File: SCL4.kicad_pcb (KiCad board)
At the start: 2 copper layers, 233.7 x 300 mm, 4 parts

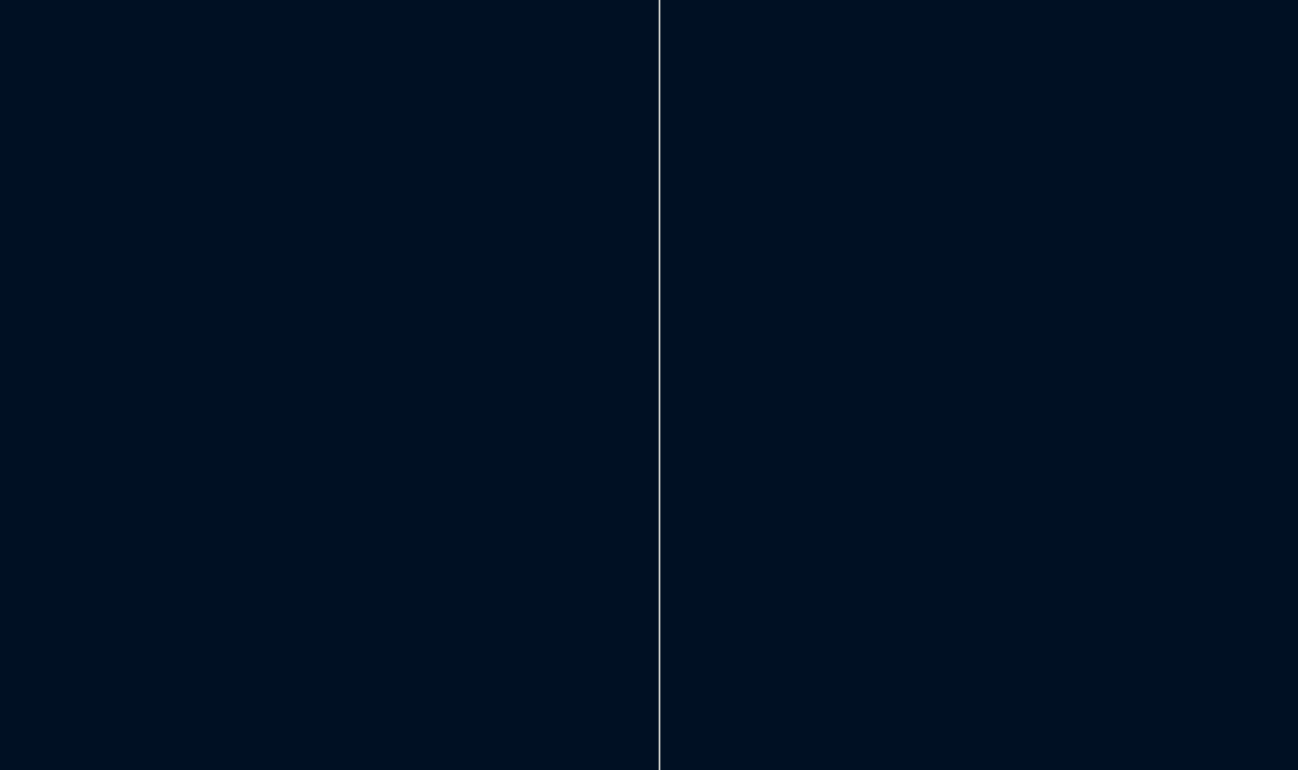
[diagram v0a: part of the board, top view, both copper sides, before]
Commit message: swap abcd on siedecon
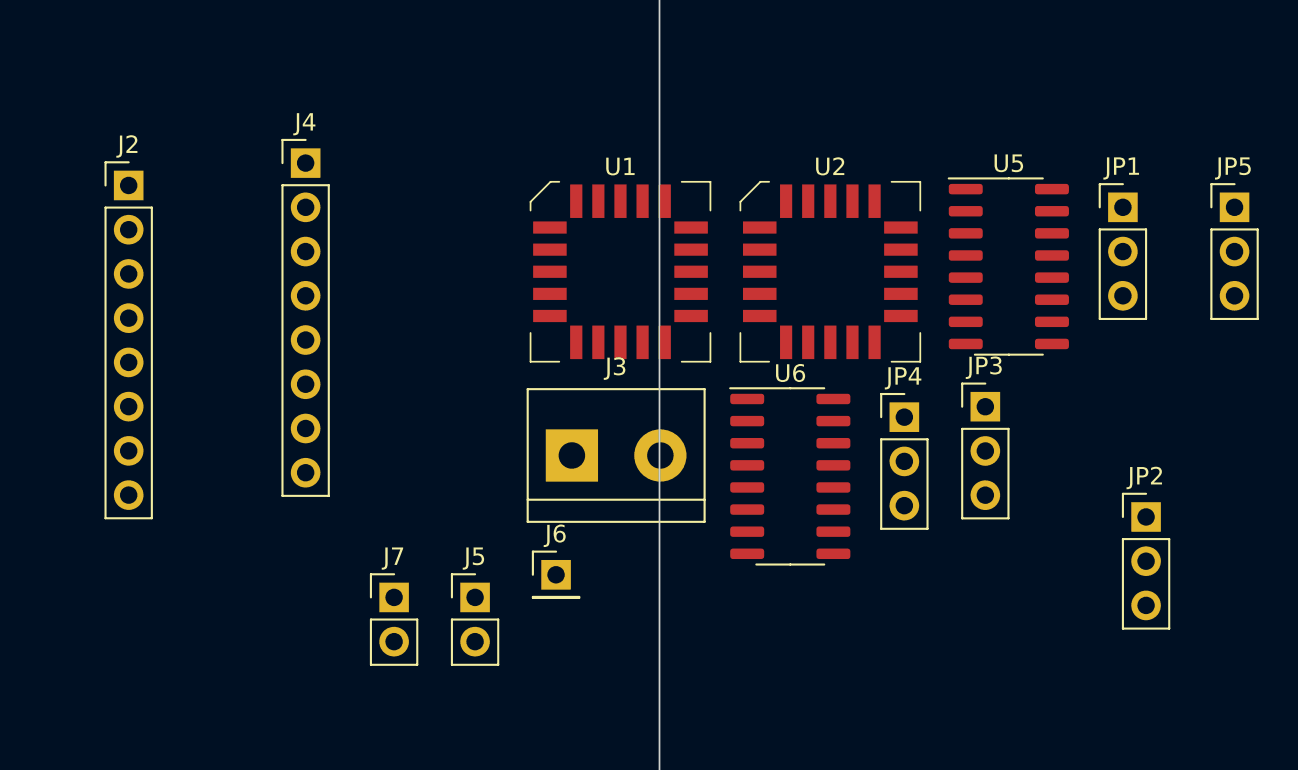
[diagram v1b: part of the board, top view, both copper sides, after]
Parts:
- added J2: Conn_01x08, Connector_PinHeader_2.54mm:PinHeader_1x08_P2.54mm_Vertical, F.Cu at (203.2, 21.6)
- added J3: 5V out, TerminalBlock:TerminalBlock_bornier-2_P5.08mm, F.Cu at (228.7, 37.1)
- added J4: spare1, Connector_PinHeader_2.54mm:PinHeader_1x08_P2.54mm_Vertical, F.Cu at (213.4, 20.3)
- added J5: SP1, Connector_PinHeader_2.54mm:PinHeader_1x02_P2.54mm_Vertical, F.Cu at (223.1, 45.3)
- added J6: spare2, Connector_PinHeader_2.54mm:PinHeader_1x01_P2.54mm_Vertical, F.Cu at (227.7, 44.0)
- added J7: SP2, Connector_PinHeader_2.54mm:PinHeader_1x02_P2.54mm_Vertical, F.Cu at (218.4, 45.3)
- added JP1: LSA, Connector_PinHeader_2.54mm:PinHeader_1x03_P2.54mm_Vertical, F.Cu at (260.3, 22.9)
- added JP2: LSB, Connector_PinHeader_2.54mm:PinHeader_1x03_P2.54mm_Vertical, F.Cu at (261.6, 40.6)
- added JP3: LOCAL, Connector_PinHeader_2.54mm:PinHeader_1x03_P2.54mm_Vertical, F.Cu at (252.4, 34.3)
- added JP4: NEXT, Connector_PinHeader_2.54mm:PinHeader_1x03_P2.54mm_Vertical, F.Cu at (247.7, 34.9)
- added JP5: SYSTEM, Connector_PinHeader_2.54mm:PinHeader_1x03_P2.54mm_Vertical, F.Cu at (266.7, 22.9)
- added U1: MC10H125 (20PLCC), Package_LCC:PLCC-20, F.Cu at (231.4, 26.6)
- added U2: MC10H124 (20PLCC), Package_LCC:PLCC-20, F.Cu at (243.5, 26.6)
- added U5: MC3487DX, Package_SO:SOIC-16_3.9x9.9mm_P1.27mm, F.Cu at (253.7, 26.3)
- added U6: MC3487DX, Package_SO:SOIC-16_3.9x9.9mm_P1.27mm, F.Cu at (241.2, 38.3)

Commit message: starting routing
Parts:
- added C2: 100uF 63V, Capacitor_THT:CP_Radial_D10.0mm_P5.00mm, F.Cu at (259.3, 182.2)
- added D1: SMCX70A, Diode_SMD:D_SMC_Handsoldering, F.Cu at (253.4, 157.5)
- added D2: SMCX70A, Diode_SMD:D_SMC_Handsoldering, F.Cu at (266.1, 149.2)
- added F1: 5A, BUSSMAN:BUSSMAN SFT-1, F.Cu at (275.0, 166.2)
- added F2: 3A, BUSSMAN:BUSSMAN SFT-1, F.Cu at (275.0, 157.9)
- added J3: Siemens_A1010-A263, SIEDECON:Siedecon 256+6, F.Cu at (291.9, 27.9)
- added L1: INDUCTOR, Inductor_THT:L_Axial_L12.8mm_D5.8mm_P20.32mm_Horizontal_Fastron_HBCC, F.Cu at (246.4, 162.6)
- added R1: 10R 2%, Resistor_THT:R_Axial_DIN0207_L6.3mm_D2.5mm_P15.24mm_Horizontal, F.Cu at (252.7, 182.9)
- added R10: 10K, Resistor_SMD:R_2816_7142Metric_Pad3.20x4.45mm_HandSolder, F.Cu at (263.5, 68.6)
- added R2: 27R, Resistor_SMD:R_1206_3216Metric_Pad1.30x1.75mm_HandSolder, F.Cu at (287.0, 228.6)
- added R3: 51R, Resistor_SMD:R_2816_7142Metric_Pad3.20x4.45mm_HandSolder, F.Cu at (263.5, 76.2)
- added R4: 51R, Resistor_SMD:R_2816_7142Metric_Pad3.20x4.45mm_HandSolder, F.Cu at (251.5, 53.3)
- added R5: 51R, Resistor_SMD:R_2816_7142Metric_Pad3.20x4.45mm_HandSolder, F.Cu at (263.5, 53.3)
- added R6: 51R, Resistor_SMD:R_2816_7142Metric_Pad3.20x4.45mm_HandSolder, F.Cu at (251.5, 61.0)
- added R7: 51R, Resistor_SMD:R_2816_7142Metric_Pad3.20x4.45mm_HandSolder, F.Cu at (251.5, 68.6)
- added R8: 51R, Resistor_SMD:R_2816_7142Metric_Pad3.20x4.45mm_HandSolder, F.Cu at (251.5, 76.2)
- added R9: 10K, Resistor_SMD:R_2816_7142Metric_Pad3.20x4.45mm_HandSolder, F.Cu at (263.5, 61.0)
- added U3: TRAM Size 2, Transputer:TRAM size 2, F.Cu at (243.8, 27.3)
- C1: renamed from C2; footprint Capacitor_THT:CP_Axial_L29.0mm_D20.0mm_P35.00mm_Horizontal -> Capacitor_THT:CP_Radial_D5.0mm_P2.50mm
- C3: renamed from C1; footprint Capacitor_THT:CP_Axial_L26.5mm_D20.0mm_P33.00mm_Horizontal -> Capacitor_THT:CP_Radial_D13.0mm_P5.00mm
- J1: renamed from J4; footprint Connector_PinHeader_2.54mm:PinHeader_1x08_P2.54mm_Vertical -> Connector_PinHeader_2.54mm:PinHeader_1x01_P2.54mm_Vertical
- moved C1 200.4 mm to (246.4, 139.7)
- moved PS1 180.2 mm to (238.7, 127.1), turned to -90 degrees
- moved PS2 149.4 mm to (264.2, 215.9), turned to -90 degrees
- moved J1 109.2 mm to (273.1, 111.8)
- moved J5 91.9 mm to (281.9, 111.8)
- moved J2 89.6 mm to (286.4, 111.8)
- moved J4 85.9 mm to (277.5, 111.8)
- moved C3 85.6 mm to (264.2, 167.6)
- moved U1 76.4 mm to (276.9, 99.1)
- moved JP3 74.4 mm to (256.5, 96.5)
- moved JP1 64.5 mm to (266.7, 96.5)
- moved JP2 62.9 mm to (261.6, 96.5)
- moved J7 62.1 mm to (180.3, 76.2), turned to -90 degrees
- moved U2 52.0 mm to (276.9, 76.2)
- moved U4 45.4 mm to (276.9, 25.4), turned to -90 degrees
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- renumbered J6 to J2, J5 to J4, J7 to J5, J2 to J6, J3 to J7, JP4 to JP1, JP3 to JP2, JP5 to JP3, JP1 to JP4, JP2 to JP5, U5 to U1, U6 to U2, U1 to U4, U2 to U5
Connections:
- C1 pad 1: +48V -> Net-(C1-Pad1)
- PS1 pad 1: +48V -> Net-(C1-Pad1)
- PS2 pad 14: Net-(PS2-Pad14) -> GND
- PS2 pad 15: Net-(PS2-Pad14) -> GND
- PS2 pad 16: Net-(PS2-Pad14) -> GND
- PS2 pad 17: unconnected-(PS2-Pad17) -> Net-(R2-Pad1)
- PS2 pad 18: -5V -> Net-(PS2-Pad18)
- PS2 pad 19: -5V -> Net-(PS2-Pad18)
- PS2 pad 20: -5V -> Net-(PS2-Pad18)
- PS2 pad 32: +48V -> +L48V
- PS2 pad 33: -48V -> -L48V
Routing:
- net GND: track 47.7 -> 787.7 mm, vias 0 -> 1
- net +5V: track 47.0 -> 473.5 mm, vias 0 -> 1
- net Net-(C1-Pad1): track 0.00 -> 116.8 mm
- net /TByte: track 0.00 -> 107.1 mm, vias 0 -> 1
- net /TL0In: track 0.00 -> 80.6 mm
- net +L48V: track 0.00 -> 77.7 mm
- net /TL0Out: track 0.00 -> 77.0 mm
- net /TNotError: track 0.00 -> 65.8 mm
- net -L48V: track 0.00 -> 60.0 mm
- net /TL2out: track 0.00 -> 49.8 mm, vias 0 -> 1
- net +48V: track 121.0 -> 71.8 mm
- net /TClk: track 0.00 -> 46.2 mm
- net //L2OUT: track 0.00 -> 40.5 mm, vias 0 -> 2
- net //L2IN: track 0.00 -> 38.6 mm, vias 0 -> 2
- net /RESET: track 0.00 -> 31.4 mm, vias 0 -> 1
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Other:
- board size 233.7 x 300 mm -> 280 x 234 mm

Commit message: board layout complete
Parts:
- R10, R3, R4, R5, R6, R7, R8, R9: footprint Resistor_SMD:R_2816_7142Metric_Pad3.20x4.45mm_HandSolder -> Resistor_SMD:R_1206_3216Metric_Pad1.30x1.75mm_HandSolder
- moved R3 46.6 mm to (268.6, 29.8), turned to 90 degrees
- moved R10 42.6 mm to (261.6, 26.0), turned to 180 degrees
- moved R5 31.5 mm to (284.5, 29.8), turned to -90 degrees
- moved R8 30.1 mm to (280.0, 66.7), turned to 180 degrees
- moved R6 28.6 mm to (280.0, 61.6), turned to 180 degrees
- moved R4 25.9 mm to (273.7, 66.7)
- moved R7 23.3 mm to (273.7, 61.6)
- moved R9 18.1 mm to (257.8, 43.8), turned to 180 degrees
- moved D2 10.8 mm to (257.8, 142.2), turned to 180 degrees
- moved D1 7.24 mm to (257.8, 151.8), turned to 180 degrees
- moved C2 6.31 mm to (265.4, 181.0), turned to 180 degrees
- moved C3 5.99 mm to (259.1, 164.5), turned to 0 degrees
- moved J7 3.81 mm to (184.2, 76.2)
- moved C1 2.62 mm to (245.7, 137.2)
- moved U3 2.54 mm to (246.4, 27.3)
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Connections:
- net +L48V renamed Net-(C2-Pad1)
- net -L48V renamed Net-(C2-Pad2)
- net Net-(J5-Pad1) renamed +5Vbig
- net Net-(JP4-Pad2) renamed /SpeedA
- net Net-(JP5-Pad2) renamed /SpeedB
- PS2 pad 1: unconnected-(PS2-Pad1) -> (no net)
- PS2 pad 10: unconnected-(PS2-Pad10) -> (no net)
- PS2 pad 11: unconnected-(PS2-Pad11) -> (no net)
- PS2 pad 12: unconnected-(PS2-Pad12) -> (no net)
- PS2 pad 13: unconnected-(PS2-Pad13) -> (no net)
- PS2 pad 18: Net-(PS2-Pad18) -> -5V
- PS2 pad 19: Net-(PS2-Pad18) -> -5V
- PS2 pad 2: unconnected-(PS2-Pad2) -> (no net)
- PS2 pad 20: Net-(PS2-Pad18) -> -5V
- PS2 pad 21: unconnected-(PS2-Pad21) -> (no net)
- PS2 pad 22: unconnected-(PS2-Pad22) -> (no net)
- PS2 pad 23: unconnected-(PS2-Pad23) -> (no net)
- PS2 pad 24: unconnected-(PS2-Pad24) -> (no net)
- PS2 pad 26: unconnected-(PS2-Pad26) -> (no net)
- PS2 pad 27: unconnected-(PS2-Pad27) -> (no net)
- PS2 pad 28: unconnected-(PS2-Pad28) -> (no net)
- PS2 pad 29: unconnected-(PS2-Pad29) -> (no net)
- PS2 pad 3: unconnected-(PS2-Pad3) -> (no net)
- PS2 pad 30: unconnected-(PS2-Pad30) -> (no net)
- PS2 pad 31: unconnected-(PS2-Pad31) -> (no net)
- PS2 pad 34: unconnected-(PS2-Pad34) -> (no net)
- PS2 pad 35: unconnected-(PS2-Pad35) -> (no net)
- PS2 pad 36: unconnected-(PS2-Pad36) -> (no net)
- PS2 pad 37: unconnected-(PS2-Pad37) -> (no net)
- PS2 pad 38: unconnected-(PS2-Pad38) -> (no net)
- PS2 pad 39: unconnected-(PS2-Pad39) -> (no net)
- PS2 pad 4: unconnected-(PS2-Pad4) -> (no net)
- PS2 pad 40: unconnected-(PS2-Pad40) -> (no net)
- PS2 pad 5: unconnected-(PS2-Pad5) -> (no net)
- PS2 pad 6: unconnected-(PS2-Pad6) -> (no net)
- PS2 pad 7: unconnected-(PS2-Pad7) -> (no net)
- PS2 pad 8: unconnected-(PS2-Pad8) -> (no net)
- PS2 pad 9: unconnected-(PS2-Pad9) -> (no net)
- R10 pad 2: Net-(R10-Pad2) -> GND
- R4 pad 2: GND -> -5V
- R6 pad 2: GND -> -5V
- R7 pad 2: GND -> -5V
- R8 pad 2: GND -> -5V
- R9 pad 2: Net-(R10-Pad2) -> GND
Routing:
- net -5V: track 28.7 -> 290.6 mm, vias 0 -> 6
- net /TReset: track 0.00 -> 140.5 mm, vias 0 -> 2
- net /TAnalyse: track 0.00 -> 137.6 mm, vias 0 -> 2
- net +5V: track 473.5 -> 600.7 mm, vias 1 -> 4
- net /TL3in: track 0.00 -> 113.2 mm, vias 0 -> 4
- net /TL3out: track 0.00 -> 99.1 mm
- net GND: track 787.7 -> 883.5 mm, vias 1 -> 6
- net Net-(JP3-Pad2): track 0.00 -> 50.3 mm, vias 0 -> 2
- net /TL2in: track 0.00 -> 49.0 mm, vias 0 -> 2
- net /TL0In: track 80.6 -> 105.8 mm
- net /TNotError: track 65.8 -> 90.3 mm, vias 0 -> 1
- net /TL0Out: track 77.0 -> 100.4 mm
- net /L2OUT: track 30.5 -> 52.2 mm, vias 2 -> 3
- net //L3OUT: track 24.7 -> 41.8 mm, vias 0 -> 2
- net -48V: track 172.0 -> 156.7 mm
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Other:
- board size 280 x 234 mm -> 127.6 x 233.3 mm
- board text added: "!ERROR"
- board text added: "+5V"
- board text added: "ANALYSE"
- board text added: "BYTE"
- board text added: "CLOCK"
- board text added: "GND"
- board text added: "L0 IN"
- board text added: "L0 OUT"
- board text added: "RESET"

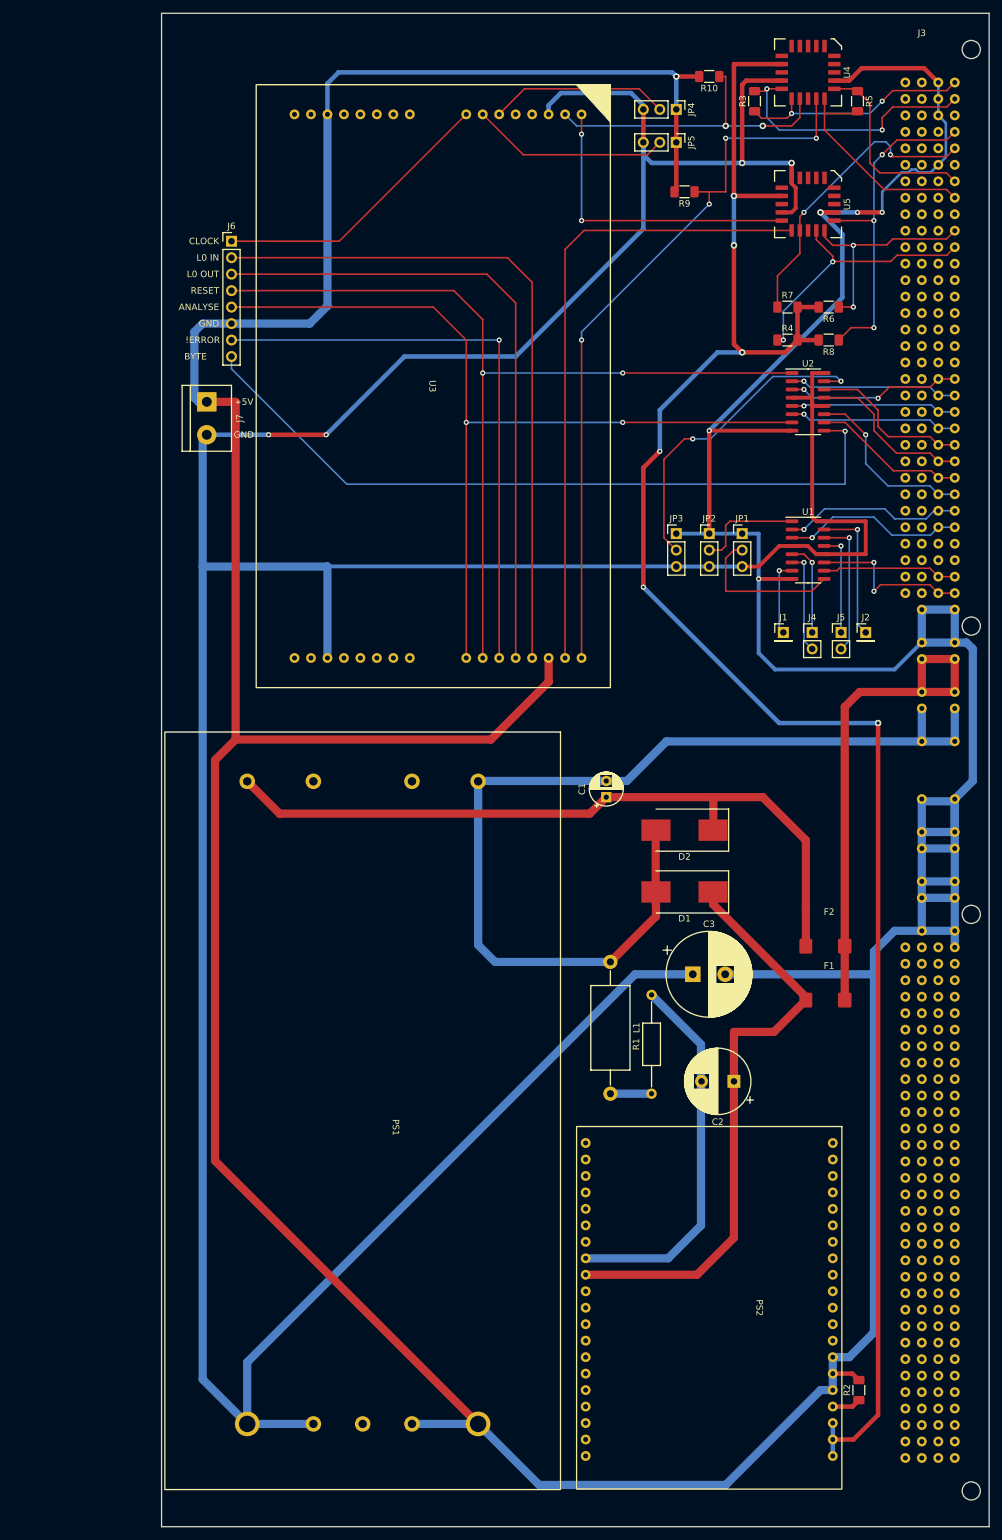
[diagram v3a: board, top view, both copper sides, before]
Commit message: fix static gnd pin
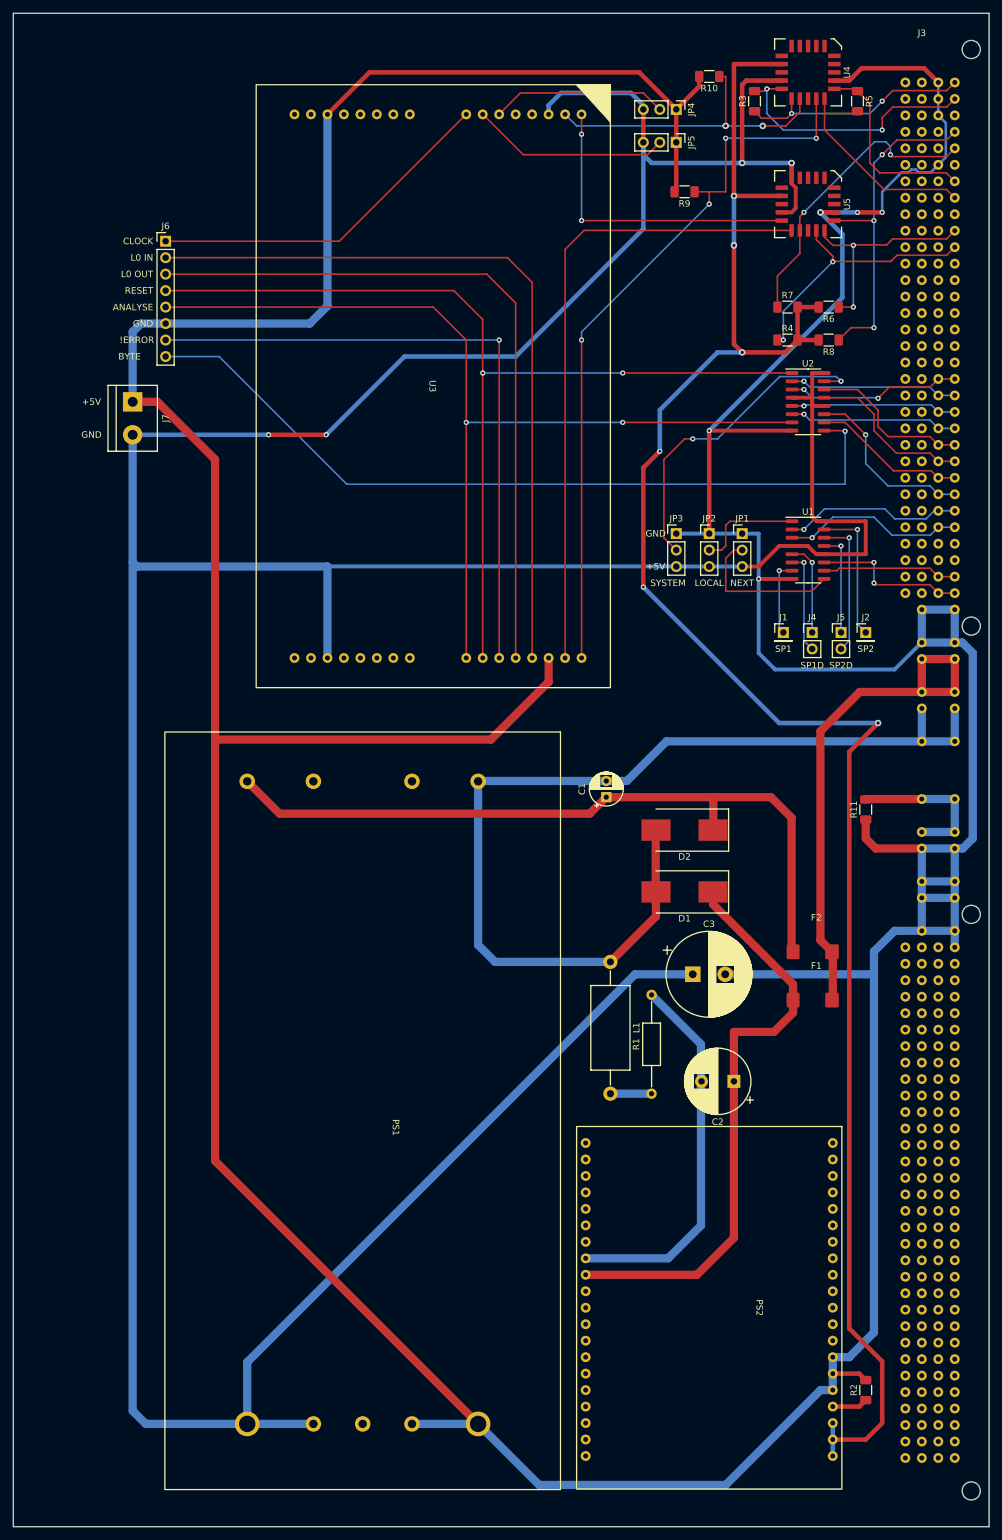
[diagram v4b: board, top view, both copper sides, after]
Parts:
- added R11: 1M, Resistor_SMD:R_1206_3216Metric_Pad1.30x1.75mm_HandSolder, F.Cu at (285.8, 139.1)
- moved J7 11.4 mm to (172.7, 76.2)
- moved J6 10.2 mm to (177.8, 51.4)
- moved F2 2.15 mm to (273.1, 158.8)
- moved F1 1.96 mm to (273.1, 166.2)
- moved R2 1.06 mm to (285.8, 228.6)
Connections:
- net +5Vbig renamed Net-(J5-Pad1)
- J3 pad P4: GND -> /Static
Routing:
- net +5V: track 600.7 -> 636.6 mm
- net /Static: track 0.00 -> 23.9 mm
- net /TReset: track 140.5 -> 150.6 mm
- net /TNotError: track 90.3 -> 100.5 mm
- net /TL0In: track 105.8 -> 116.0 mm
- net /TClk: track 44.3 -> 54.5 mm
- net /TL0Out: track 100.4 -> 110.6 mm
- net /TAnalyse: track 137.6 -> 147.7 mm
- net /TByte: track 115.3 -> 124.4 mm
- net -5V: track 290.6 -> 295.9 mm
- net +48V: track 78.4 -> 80.7 mm
- net Net-(C2-Pad1): track 92.7 -> 91.1 mm
- net //NEXT: track 25.5 -> 24.0 mm
- net Net-(PS2-Pad17): track 4.43 -> 5.49 mm
- net Net-(C1-Pad1): track 113.4 -> 114.2 mm
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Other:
- board size 127.6 x 233.3 mm -> 150.5 x 233.3 mm
- board text added: "LOCAL"
- board text added: "NEXT"
- board text added: "SP1"
- board text added: "SP1D"
- board text added: "SP2"
- board text added: "SP2D"
- board text added: "SYSTEM"

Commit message: polish
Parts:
- moved R5 3.86 mm to (283.8, 33.7)
- moved R10 3.59 mm to (259.1, 23.5)
- moved R3 1.42 mm to (267.3, 30.5)
- moved R11 1.27 mm to (285.8, 140.3)
- moved C2 1.27 mm to (265.4, 179.7)
- moved R9 0.63 mm to (258.4, 43.8)
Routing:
- net /TL3out: track 99.1 -> 89.5 mm
- net Net-(JP3-Pad2): track 50.3 -> 58.3 mm
- net /LOCAL: track 27.6 -> 34.1 mm
- net Net-(JP1-Pad2): track 24.1 -> 30.4 mm
- net //L2OUT: track 46.3 -> 51.9 mm
- net /Static: track 23.9 -> 29.5 mm
- net //ANALYSE: track 25.6 -> 31.0 mm
- net /ANALYSE: track 26.0 -> 31.2 mm
- net /RESET: track 26.0 -> 31.2 mm
- net //RESET: track 26.9 -> 32.1 mm
- net -48V: track 156.7 -> 161.8 mm
- net Net-(J4-Pad1): track 14.4 -> 18.5 mm
- net Net-(J4-Pad2): track 15.7 -> 19.8 mm
- net //LOCAL: track 28.1 -> 32.0 mm
- net Net-(C2-Pad1): track 91.1 -> 87.8 mm
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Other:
- board text added: "LINK IN"
- board text added: "LINK OUT"
- board text removed: "L0 IN"
- board text removed: "L0 OUT"

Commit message: fix pin numbering of vicor
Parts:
- moved R9 1.42 mm to (257.8, 45.1)
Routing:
- net -48V: track 161.8 -> 220.9 mm
- net Net-(C1-Pad1): track 114.2 -> 78.6 mm
- net GND: track 882.2 -> 910.6 mm
- net +5V: track 638.9 -> 625.5 mm
- net /TL3in: track 112.2 -> 113.3 mm
